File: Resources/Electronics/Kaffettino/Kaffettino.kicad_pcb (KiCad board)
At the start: 2 copper layers, 150 x 150 mm, 36 parts, among them J2 OSTVN02A150, J3 OSTVN04A150, J4 OSTVN04A150, J5 OSTVN04A150, M1 RFID-RC522, U1 PCF8574AN, U2 DFR0299, U3 ESP32-38Pin-Wroom, U4 26052

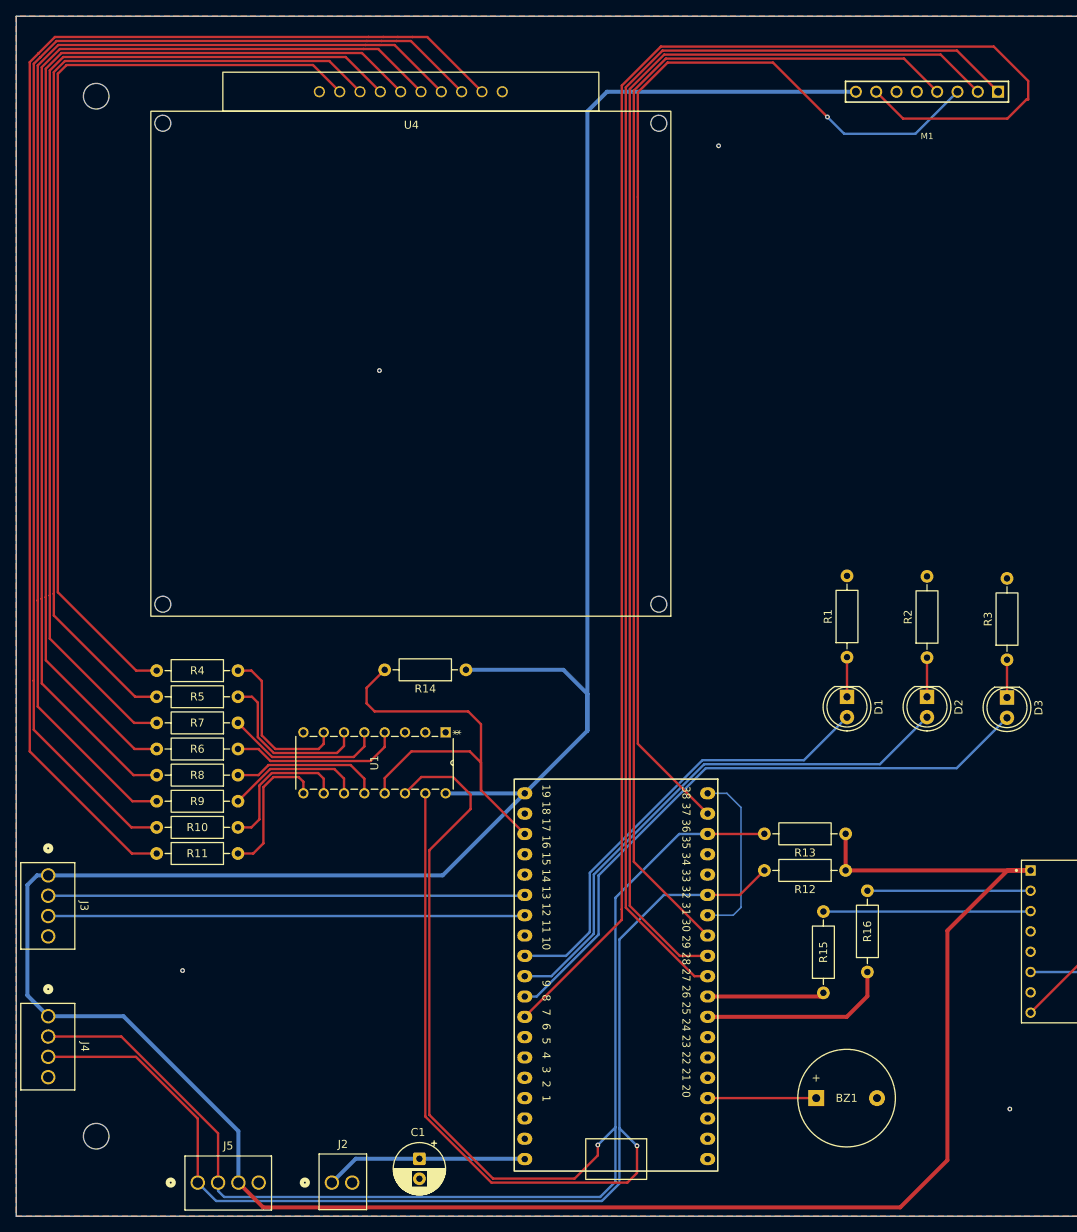
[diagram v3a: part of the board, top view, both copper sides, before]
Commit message: Embedded: fixed some footprints in the PCB design, started working on keyEvents.
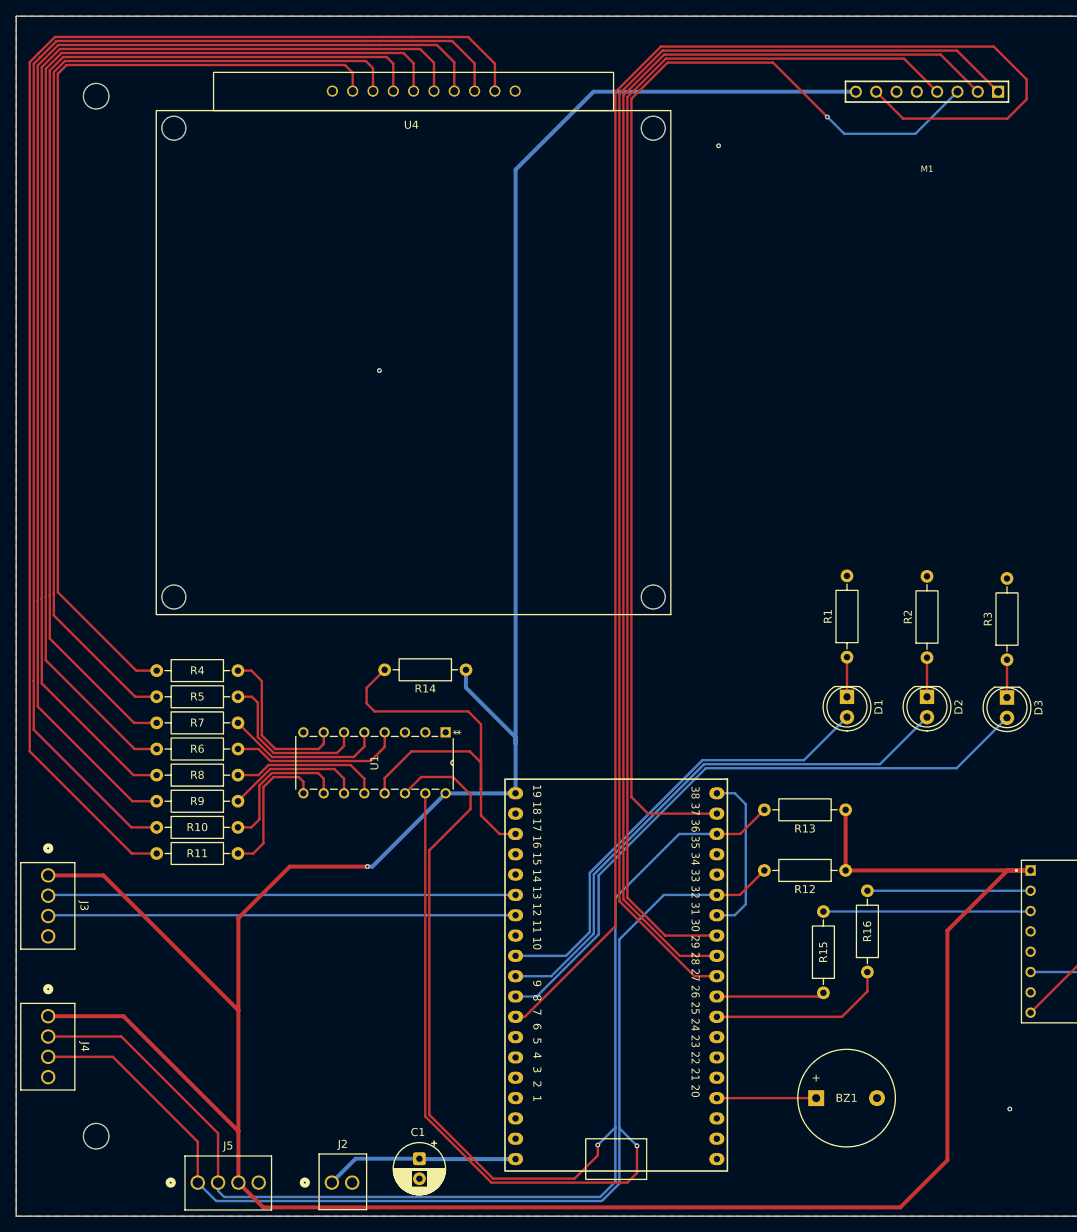
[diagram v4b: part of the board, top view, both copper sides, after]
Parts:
- moved R13 3.00 mm to (123.7, 114.2)
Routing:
- net /RFID_MOSI: track 141.1 -> 147.3 mm
- net /RFID_MISO: track 150.7 -> 155.6 mm
- net Net-(U4-C3): track 153.8 -> 157.5 mm
- net Net-(U4-C4): track 146.7 -> 150.4 mm
- net Net-(U4-R1): track 139.6 -> 143.2 mm
- net Net-(U4-C2): track 161.0 -> 164.6 mm
- net Net-(U4-R2): track 132.6 -> 136.1 mm
- net Net-(U4-C1): track 168.0 -> 171.6 mm
- net Net-(U4-R3): track 125.4 -> 128.7 mm
- net Net-(U4-R4): track 118.3 -> 121.2 mm
- net /RFID_SCK: track 161.6 -> 163.4 mm
- net /RFID_SDA: track 166.9 -> 168.7 mm
- net /GEN_SDA: track 213.9 -> 212.3 mm
- net /MICRO_SD_RX: track 24.1 -> 22.6 mm
- net /GEN_SCL: track 223.7 -> 225.0 mm
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
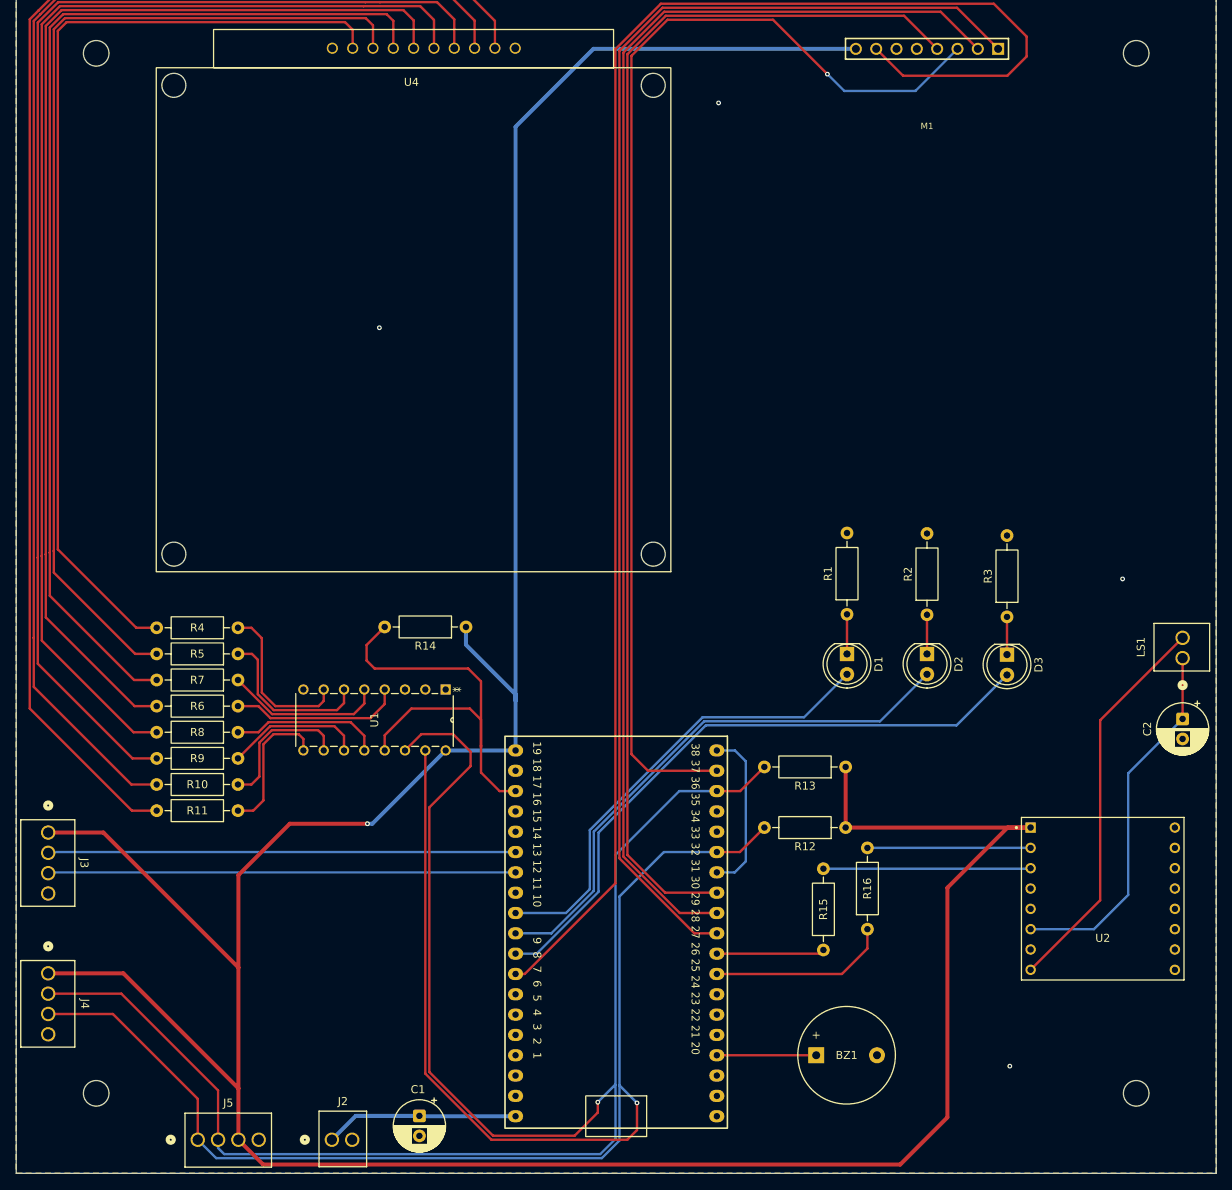
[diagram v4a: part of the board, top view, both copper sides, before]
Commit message: Embedded: Finished developing PCB, fixed grb and drill files, added silkscreen.
TODO: Check correctness of footprints and NPN Junction.
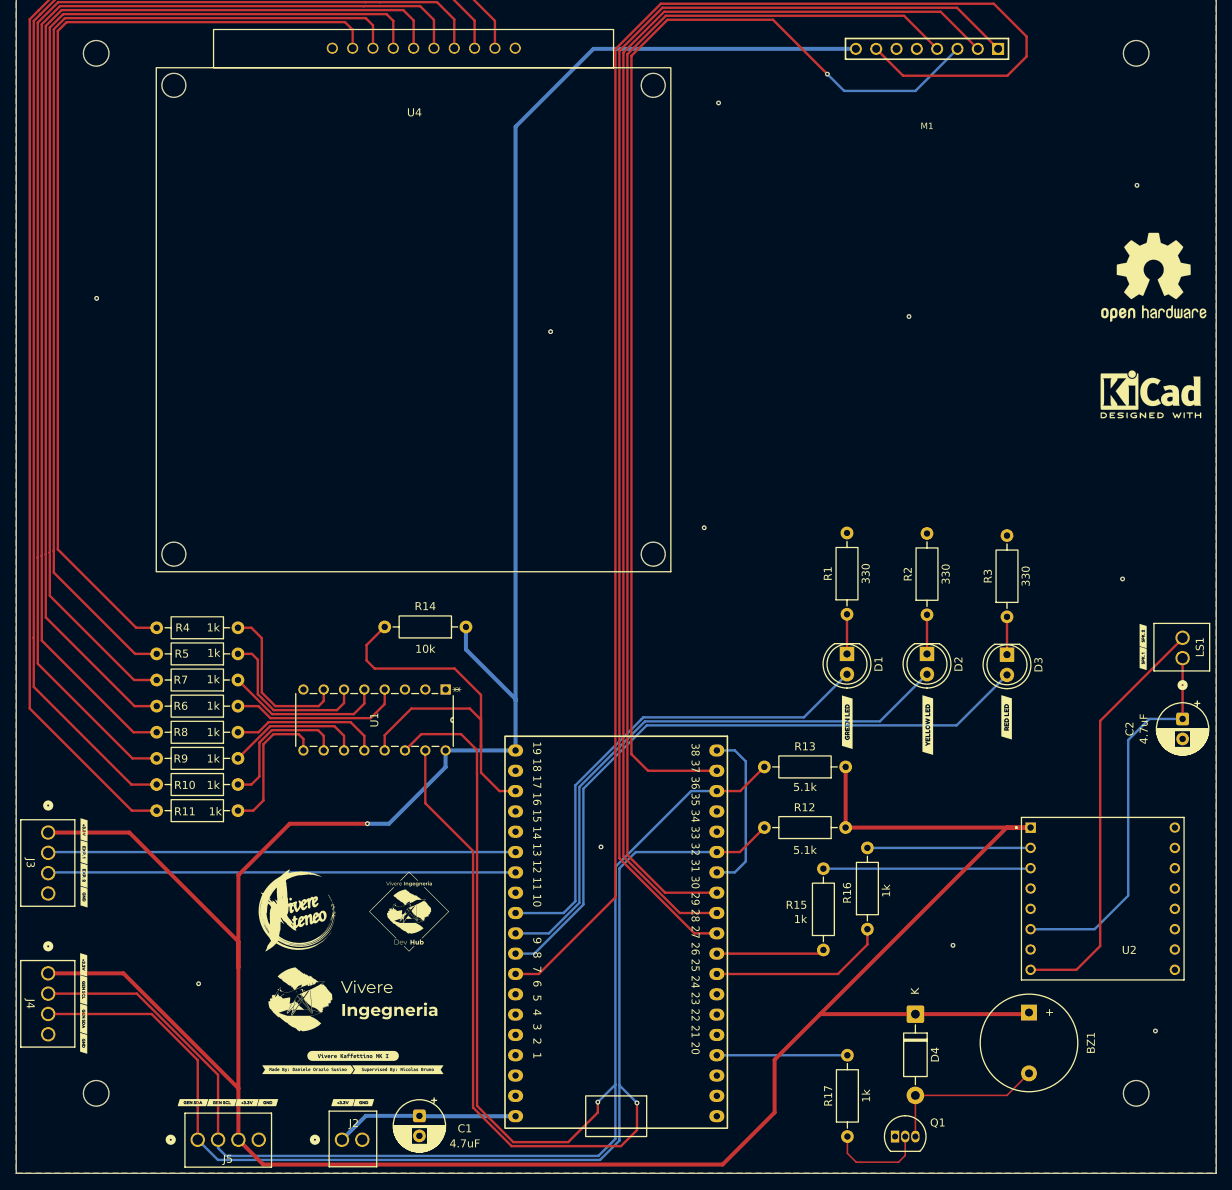
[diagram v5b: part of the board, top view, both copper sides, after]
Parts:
- added D4: 1N4001, Diode_THT:D_DO-41_SOD81_P10.16mm_Horizontal, F.Cu at (132.4, 145.1)
- added G***: LOGO, Images:Logo-VivereAteneo, F.Cu at (55.2, 132.1)
- added G***: LOGO, Images:Logo-VivereIngegneria, F.Cu at (62.2, 143.3)
- added G***: LOGO, Images:Logo-VivereDevHub, F.Cu at (69.1, 132.3)
- added Q1: PN2222A, Package_TO_SOT_THT:TO-92_Inline, F.Cu at (129.9, 160.4)
- added R17: 1k, Resistor_THT:R_Axial_DIN0207_L6.3mm_D2.5mm_P10.16mm_Horizontal, F.Cu at (123.9, 160.4)
- added REF**: KiCad-Logo2_5mm_SilkScreen, Symbol:KiCad-Logo2_5mm_SilkScreen, F.Cu at (161.8, 67.6)
- added REF**: OSHW-Logo2_14.6x12mm_SilkScreen, Symbol:OSHW-Logo2_14.6x12mm_SilkScreen, F.Cu at (162.2, 53.0)
- added kibuzzard-69A0B975: G***, kibuzzard-69A0B975, F.Cu at (62.1, 150.3)
- added kibuzzard-69A0B9A7: G***, kibuzzard-69A0B9A7, F.Cu at (67.7, 152.0)
- added kibuzzard-69A0BA46: G***, kibuzzard-69A0BA46, F.Cu at (56.5, 152.0)
- added kibuzzard-69A0D4B7: G***, kibuzzard-69A0D4B7, F.Cu at (51.4, 156.2)
- added kibuzzard-69A0D4B7: G***, kibuzzard-69A0D4B7, F.Cu at (28.5, 130.5)
- added kibuzzard-69A0D4B7: G***, kibuzzard-69A0D4B7, F.Cu at (28.4, 148.7)
- added kibuzzard-69A0D4B7: G***, kibuzzard-69A0D4B7, F.Cu at (63.4, 156.2)
- added kibuzzard-69A0D4BD: G***, kibuzzard-69A0D4BD, F.Cu at (28.4, 138.9)
- added kibuzzard-69A0D4BD: G***, kibuzzard-69A0D4BD, F.Cu at (48.9, 156.2)
- added kibuzzard-69A0D4BD: G***, kibuzzard-69A0D4BD, F.Cu at (60.8, 156.2)
- added kibuzzard-69A0D4BD: G***, kibuzzard-69A0D4BD, F.Cu at (28.5, 122.1)
- added kibuzzard-69A0D4C4: G***, kibuzzard-69A0D4C4, F.Cu at (45.7, 156.2)
- added kibuzzard-69A0D4C4: G***, kibuzzard-69A0D4C4, F.Cu at (28.4, 142.1)
- added kibuzzard-69A0D4CC: G***, kibuzzard-69A0D4CC, F.Cu at (28.4, 145.7)
- added kibuzzard-69A0D4CC: G***, kibuzzard-69A0D4CC, F.Cu at (42.1, 156.2)
- added kibuzzard-69A0D614: G***, kibuzzard-69A0D614, F.Cu at (28.5, 124.9)
- added kibuzzard-69A0D627: G***, kibuzzard-69A0D627, F.Cu at (28.5, 127.8)
- added kibuzzard-69A0D881: G***, kibuzzard-69A0D881, F.Cu at (160.9, 100.6)
- added kibuzzard-69A0D88A: G***, kibuzzard-69A0D88A, F.Cu at (160.9, 97.8)
- added kibuzzard-69A0DE3E: G***, kibuzzard-69A0DE3E, F.Cu at (123.9, 108.6)
- added kibuzzard-69A0DE44: G***, kibuzzard-69A0DE44, F.Cu at (133.9, 109.0)
- added kibuzzard-69A0DE4A: G***, kibuzzard-69A0DE4A, F.Cu at (143.8, 108.0)
- R12, R13: value 1k -> 5.1k
- moved BZ1 27.1 mm to (146.6, 144.9), turned to -90 degrees
- moved J2 1.26 mm to (60.7, 160.8)
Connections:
- BZ1 pad 1: /BUZZER -> +3.3V
- BZ1 pad 2: GNDREF -> Net-(BZ1--)
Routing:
- net Net-(BZ1--): track 0.00 -> 21.0 mm
- net +3.3V: track 436.2 -> 452.6 mm
- net Net-(Q1-B): track 0.00 -> 12.0 mm
- net /GEN_SDA: track 212.3 -> 217.0 mm
- net /GREEN: track 58.1 -> 62.3 mm
- net /YELLOW: track 69.2 -> 73.3 mm
- net /RED: track 80.2 -> 84.3 mm
- net /BUZZER: track 12.4 -> 16.3 mm
- net /GEN_SCL: track 225.0 -> 221.4 mm
- net Net-(U2-SPK2): track 49.4 -> 52.8 mm
- net Net-(U2-SPK1): track 46.4 -> 48.9 mm
- net +5V: track 24.2 -> 23.0 mm
- net /RFID_RST: track 200.6 -> 201.6 mm
- net /KP_INT: track 56.8 -> 55.8 mm
- net GNDREF: vias 4 -> 11
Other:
- board text added: "AI - Actually Indians API - A Person in India LLM - Low-cost Labour in Mumbai AGI - A Genius Indian GPT - Gujjarati Professional Typist"
- board text added: "Crazy? I was crazy once. They locked me in a room. A rubber room. A rubber room with rats. And rats make me crazy."
- board text added: "Did I ever tell you what the definition of insanity is? Insanity is doing the exact... same fucking thing... over and over again expecting... shit to change... That. Is. Crazy. Did I ever tell you what the definition of insanity is?"
- board text added: "Facciamo un kaffettino? È l'ora del kaffettino! Non dovrei, ne ho bevuti un casino! Ma io voglio seguire il mio cuoricino... VAIIIIII!"
- board text added: "Roses are #FF0000 Violets are #0000FF We just got an exception on line 42!"
- board text added: "We would like to thank the students of Vivere Ateneo and Vivere Ingegneria for allowing us to dedicate ourselves to this project <3"
- board text added: "Why do programmers prefer dark mode? Because light attracts bugs."
- board text added: "susino.dev objexlabs.com msworks.it"
- board text added: "{dblquote}I'm a full stack developer{dblquote} {dblquote}The stack: Claude.ai{dblquote}"

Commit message: Embedded: Switched buzzer from 15 (strapping pin) to 33, reflected the changes in the PCB
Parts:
- removed REF**: KiCad-Logo2_5mm_SilkScreen, Symbol:KiCad-Logo2_5mm_SilkScreen
- removed REF**: OSHW-Logo2_14.6x12mm_SilkScreen, Symbol:OSHW-Logo2_14.6x12mm_SilkScreen
- removed kibuzzard-69A0B975: G***, kibuzzard-69A0B975
- removed kibuzzard-69A0B9A7: G***, kibuzzard-69A0B9A7
- removed kibuzzard-69A0BA46: G***, kibuzzard-69A0BA46
- added kibuzzard-69A188C8: G***, kibuzzard-69A188C8, F.Cu at (139.0, 156.8)
- added kibuzzard-69A188E1: G***, kibuzzard-69A188E1, F.Cu at (128.5, 162.1)
- added kibuzzard-69A188E6: G***, kibuzzard-69A188E6, F.Cu at (150.2, 162.1)
- moved G*** 95.3 mm to (157.3, 147.8)
- moved BZ1 87.2 mm to (59.7, 137.3), turned to 0 degrees
- moved G*** 85.3 mm to (139.0, 147.8)
- moved D4 79.9 mm to (52.9, 137.3)
- moved G*** 59.2 mm to (126.2, 147.8)
- moved Q1 56.8 mm to (74.6, 147.4), turned to 180 degrees
- moved R17 54.5 mm to (73.3, 140.1)
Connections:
- U3 pad 12: unconnected-(U3-GPIO33-Pad12) -> /BUZZER
- U3 pad 23: /BUZZER -> unconnected-(U3-GPIO15-Pad23)
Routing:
- net +3.3V: track 452.6 -> 439.2 mm
- net Net-(BZ1--): track 21.0 -> 31.3 mm
- net /BUZZER: track 16.3 -> 9.08 mm
- net Net-(Q1-B): track 12.0 -> 7.34 mm
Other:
- board text added: "{dblquote}Facciamo un kaffettino? È l'ora del kaffettino! Non dovrei, ne ho bevuti un casino! Ma io voglio seguire il mio cuoricino... VAIIIIII!{dblquote} - Pupetti Tutti Matti"
- board text added: "{dblquote}I'm a full stack developer{dblquote} The stack: Claude.ai"
- board text removed: "Facciamo un kaffettino? È l'ora del kaffettino! Non dovrei, ne ho bevuti un casino! Ma io voglio seguire il mio cuoricino... VAIIIIII!"
- board text removed: "{dblquote}I'm a full stack developer{dblquote} {dblquote}The stack: Claude.ai{dblquote}"
